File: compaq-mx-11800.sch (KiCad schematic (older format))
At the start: 241 parts, among them J1 Conn_01x16_Female, J2 Conn_01x16_Female

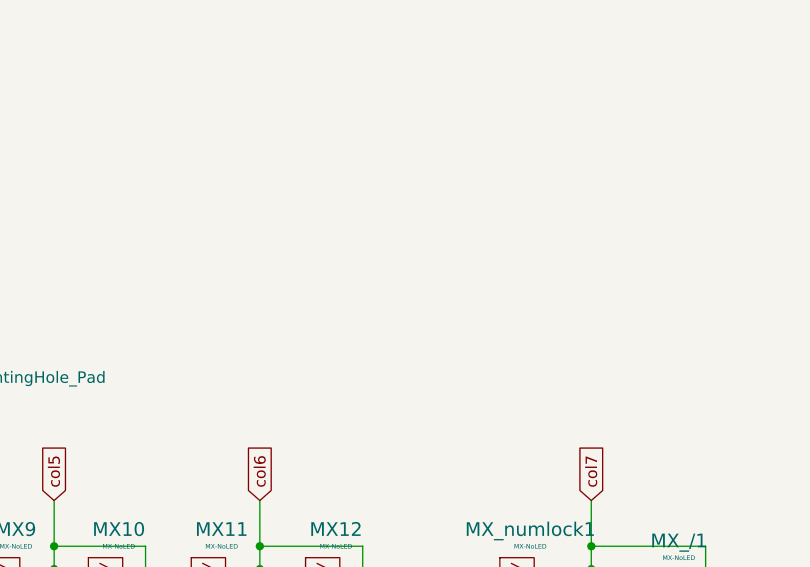
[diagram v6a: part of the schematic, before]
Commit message: add footprint for 3mm diode and add footprints to pcb
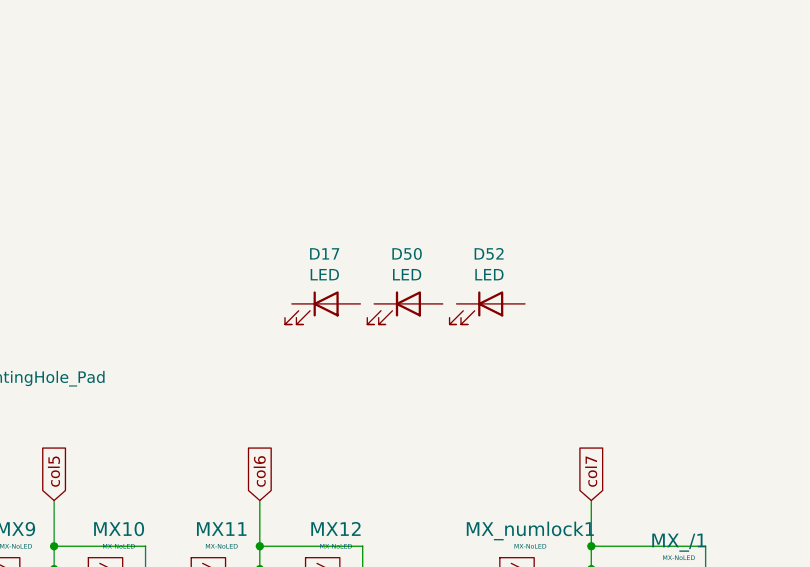
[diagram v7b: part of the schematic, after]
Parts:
- added D17, D50, D52: LED, Keebio-Parts:LED_D2.00mm, symbol Device:LED
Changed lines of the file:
@@
 Wire Wire Line
 	12340 7310 12340 7370
+$Comp
+L Device:LED D17
+U 1 1 61E5A842
+P 14940 6890
+F 0 "D17" H 14933 7107 50  0000 C CNN
+F 1 "LED" H 14933 7016 50  0000 C CNN
+F 2 "Keebio-Parts:LED_D2.00mm" H 14940 6890 50  0001 C CNN
+F 3 "~" H 14940 6890 50  0001 C CNN
+	1    14940 6890
+	1    0    0    -1
+$EndComp
+$Comp
+L Device:LED D50
+U 1 1 61E5CB9F
+P 15300 6890
+F 0 "D50" H 15293 7107 50  0000 C CNN
+F 1 "LED" H 15293 7016 50  0000 C CNN
+F 2 "Keebio-Parts:LED_D2.00mm" H 15300 6890 50  0001 C CNN
+F 3 "~" H 15300 6890 50  0001 C CNN
+	1    15300 6890
+	1    0    0    -1
+$EndComp
+$Comp
+L Device:LED D52
+U 1 1 61E5D4D7
+P 15660 6890
+F 0 "D52" H 15653 7107 50  0000 C CNN
+F 1 "LED" H 15653 7016 50  0000 C CNN
+F 2 "Keebio-Parts:LED_D2.00mm" H 15660 6890 50  0001 C CNN
+F 3 "~" H 15660 6890 50  0001 C CNN
+	1    15660 6890
+	1    0    0    -1
+$EndComp
 $EndSCHEMATC

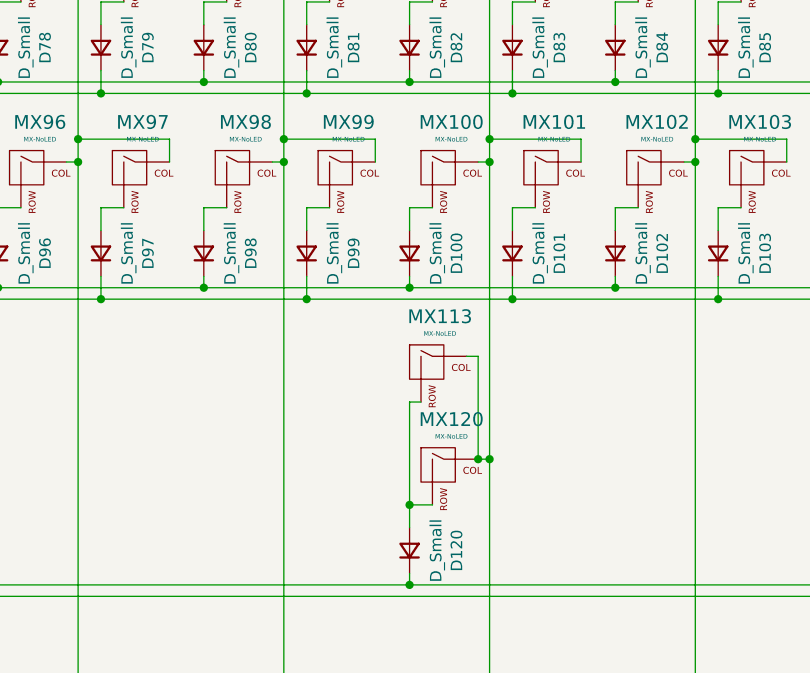
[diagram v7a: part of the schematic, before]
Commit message: mark bottom row and iso enter + align led diodes
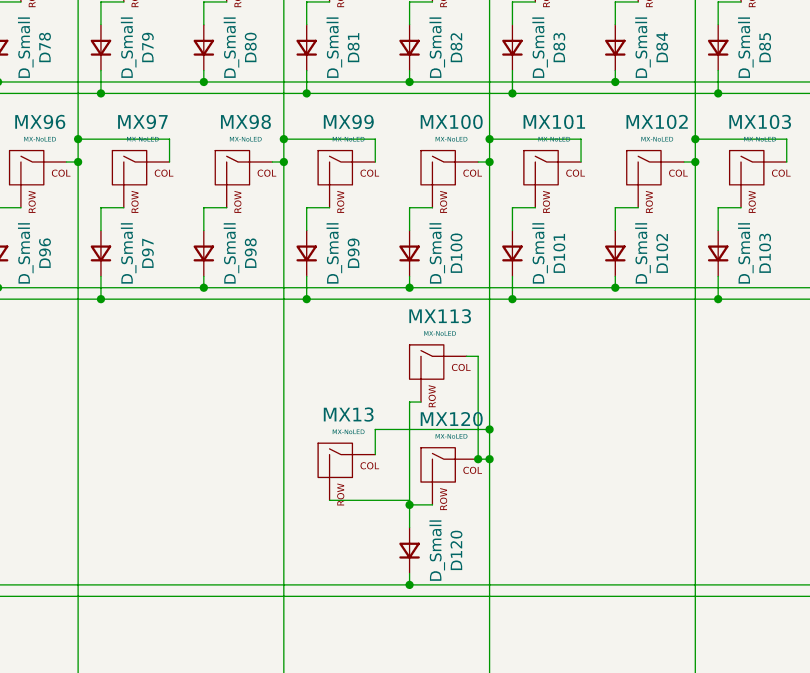
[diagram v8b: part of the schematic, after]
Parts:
- added MX13: MX-NoLED, MX_Only:MXOnly-7U-NoLED, symbol MX_Alps_Hybrid:MX-NoLED
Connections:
- wire segments 780 -> 785
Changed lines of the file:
@@
 Wire Wire Line
 	14350 10350 14250 10350
-Wire Wire Line
-	11950 12700 11950 14000
-Wire Wire Line
-	11600 13750 11600 14200
 Connection ~ 11600 14200
 Wire Wire Line
@@
 	1    0    0    -1
 $EndComp
+$Comp
+L MX_Alps_Hybrid:MX-NoLED MX13
+U 1 1 61EA3F4E
+P 11300 14030
+F 0 "MX13" H 11333 14253 60  0000 C CNN
+F 1 "MX-NoLED" H 11333 14179 20  0000 C CNN
+F 2 "MX_Only:MXOnly-7U-NoLED" H 10675 14005 60  0001 C CNN
+F 3 "" H 10675 14005 60  0001 C CNN
+	1    11300 14030
+	1    0    0    -1
+$EndComp
+Wire Wire Line
+	11450 13980 11450 13870
+Wire Wire Line
+	11450 13870 11950 13870
+Connection ~ 11950 13870
+Wire Wire Line
+	11950 13870 11950 14000
+Wire Wire Line
+	11600 13750 11600 14200
+Wire Wire Line
+	11600 14180 11600 14200
+Wire Wire Line
+	11250 14180 11600 14180
+Wire Wire Line
+	11950 12700 11950 13870
 $EndSCHEMATC
